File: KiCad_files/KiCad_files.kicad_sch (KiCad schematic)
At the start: 54 parts, among them J1 Conn_01x02_Socket, J10 Conn_01x01_Pin, J11 Conn_01x01_Pin, J6 Conn_01x01_Socket, J7 Conn_01x01_Socket, J8 Conn_01x01_Socket, J9 Conn_01x01_Socket, SW1 SW_Omron_B3FS, U2 LM22670QMR-5.0, U3 MC33275ST-3.3T3G, U4 ADM3488ExR

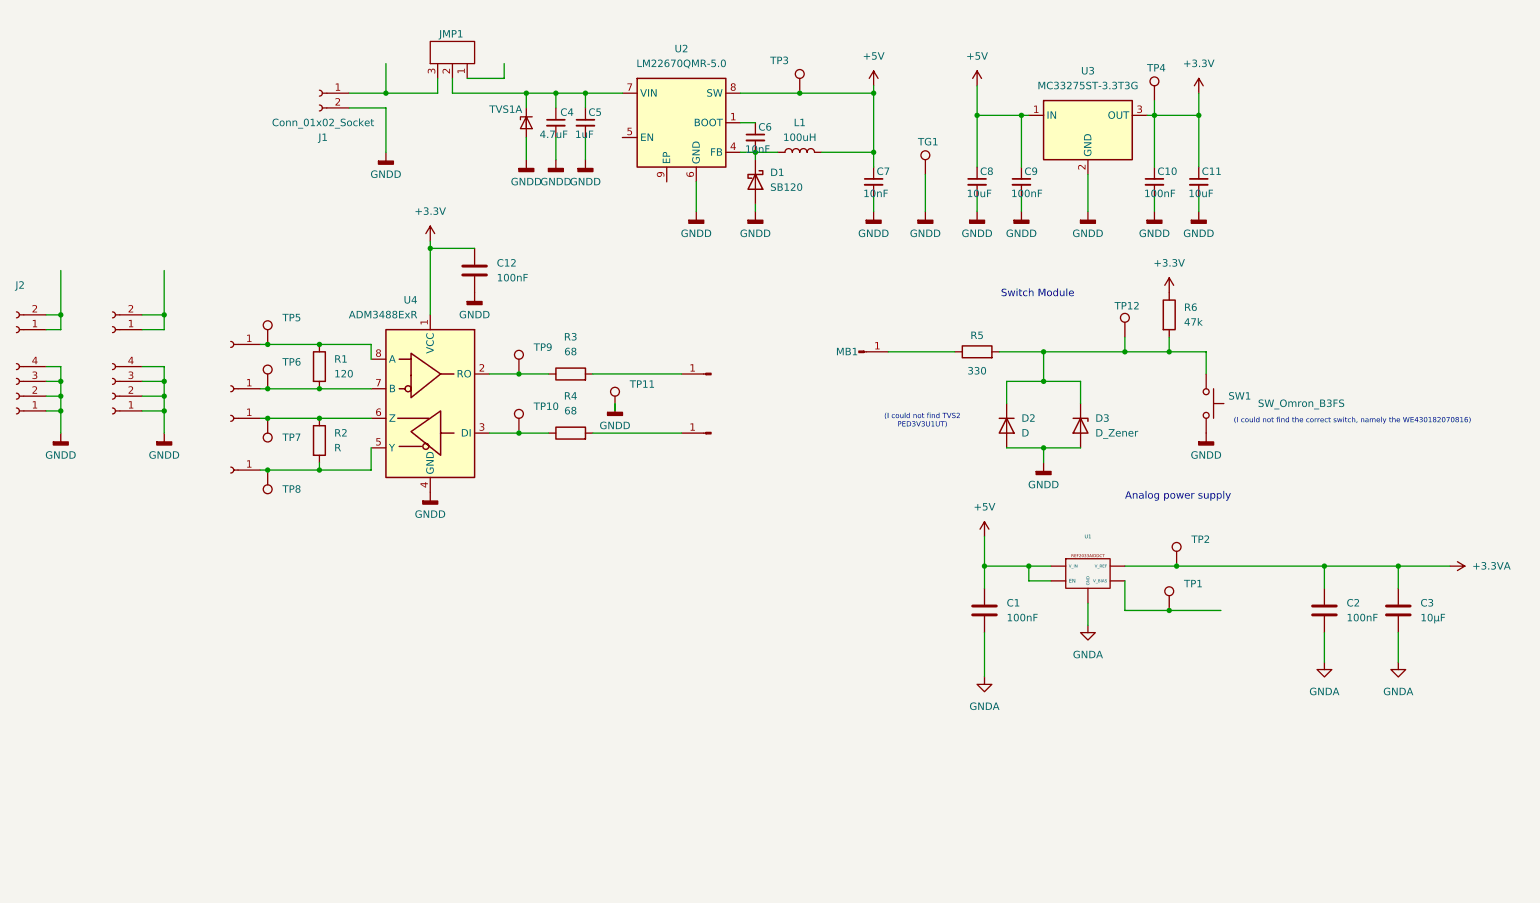
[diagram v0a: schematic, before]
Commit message: Made the schematic somewhat presentable and filled out the last bit of the circuit
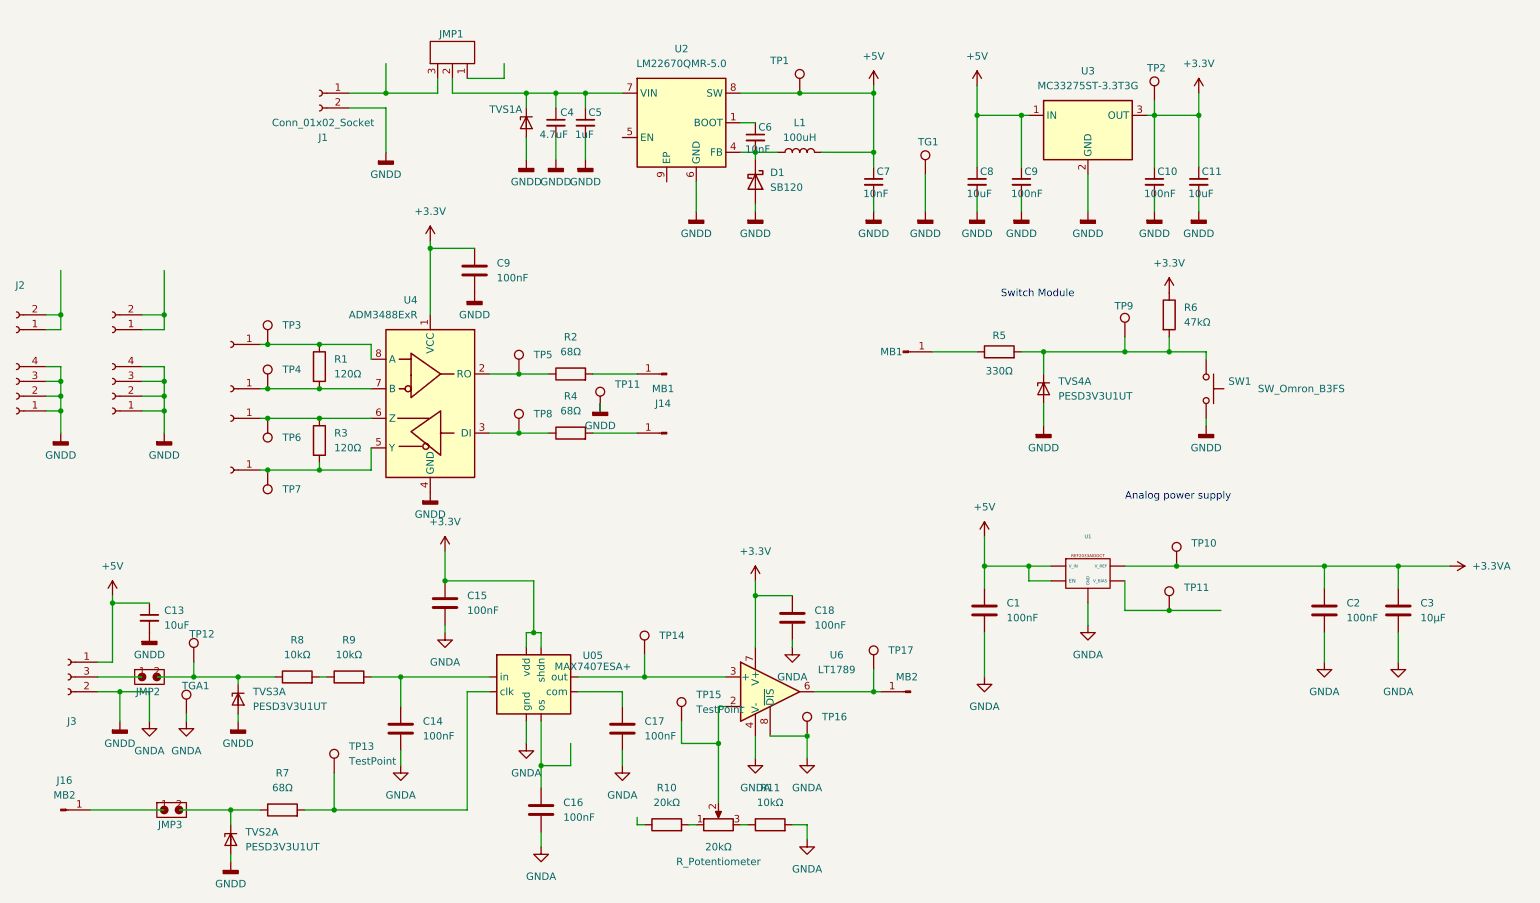
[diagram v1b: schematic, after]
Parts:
- removed D2: D, symbol Device:D
- removed D3: D_Zener, symbol Device:D_Zener
- added 20kΩ: R_Potentiometer, symbol Device:R_Potentiometer
- added C13: 10uF, symbol Device:C_Small
- added C14, C15, C16, C17, C18: 100nF, symbol Device:C
- added J16: MB2, symbol Connector:Conn_01x01_Pin
- added J3: Conn_01x03_Socket, symbol Connector:Conn_01x03_Socket
- added JMP2, JMP3: ~, symbol New_Library:2pin_jumper
- added MB2: Conn_01x01_Pin, symbol Connector:Conn_01x01_Pin
- added R10: 20kΩ, symbol Device:R
- added R11, R8, R9: 10kΩ, symbol Device:R
- added R7: 68Ω, symbol Device:R
- added TGA1, TP12, TP13, TP14, TP15, TP16, TP17: TestPoint, symbol Connector:TestPoint
- added TVS2, TVS3, TVS4: PESD3V3U1UT, Package_TO_SOT_SMD:SOT-23, symbol Power_Protection:PESD3V3L4UF
- added U6: LT1789, Package_SO:SOIC-8_3.9x4.9mm_P1.27mm, symbol Amplifier_Operational:OPA690xD
- J13: renamed from J11; value Conn_01x01_Pin -> MB1
- J14: renamed from J10; value Conn_01x01_Pin -> MB1
- R1: value 120 -> 120Ω
- R2: renamed from R3; value 68 -> 68Ω
- R3: renamed from R2; value R -> 120Ω
- R4: value 68 -> 68Ω
- R5: value 330 -> 330Ω
- R6: value 47k -> 47kΩ
- renumbered C12 to C9, TP3 to TP1, TP2 to TP10, TP1 to TP11, TP4 to TP2, TP5 to TP3, TP6 to TP4, TP9 to TP5, TP7 to TP6, TP8 to TP7, TP10 to TP8, TP12 to TP9
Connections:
- net GNDD is gone; now on net GNDA: C10.2, C11.2, C4.2, C5.2, C7.2, C8.2, C9.2, C9.2, D1.2 (A), J1.2 (Pin_2), J3.1 (Pin_1), J3.2 (Pin_2), J3.3 (Pin_3), J3.4 (Pin_4), J5.1 (Pin_1), J5.2 (Pin_2), J5.3 (Pin_3), J5.4 (Pin_4), SW1.2, TG1.1, TP11.1, TVS1.2 (A), TVS1.5 (A), U2.6 (GND), U3.2 (GND), U4.4 (GND)
- net +3.3V: now also C15.1, C18.1, U6.7 (V+)
- net +5V: now also C13.1, J3.1 (Pin_1)
- net GNDA: now also C13.2, C14.2, C15.2, C16.2, C17.2, C18.2, J3.2 (Pin_3), R11.2, TGA1.1, TP16.1, TVS2.2 (A), TVS2.5 (A), TVS3.2 (A), TVS3.5 (A), TVS4.2 (A), TVS4.5 (A), U6.4 (V-), U6.8 (~{DIS})
- net at R5.2, R6.2, SW1.1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: now also TVS4.1 (K1)
- new net: JMP3.2, R7.1, TVS2.1 (K1)
- new net: J3.3 (Pin_2), JMP2.1
- new net: JMP2.2, R8.1, TP12.1, TVS3.1 (K1)
- new net: MB2.1 (Pin_1), TP17.1, U6.6
- new net: R7.2, TP13.1
- new net: J16.1 (Pin_1), JMP3.1
- new net: R8.2, R9.1
- new net: 20kΩ.2, TP15.1, U6.2 (-)
- new net: TP14.1, U6.3 (+)
- new net: 20kΩ.3, R11.1
- new net: 20kΩ.1, R10.2
- new net: C14.1, R9.2
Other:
- note removed: "(I could not find TVS2 PED3V3U1UT)"
- note removed: "(I could not find the correct switch, namely the WE430182070816)"
- moved on the sheet: MB1, R5, SW1, TP11

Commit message: SchematicEdits
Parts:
- added J10, J8, J9: MB1, symbol Connector:Conn_01x01_Pin
- added J10, J8, J9: MB2, symbol Connector:Conn_01x01_Pin
- added TP18: 5V, symbol Connector:TestPoint
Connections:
- net GNDA: now also J8.1 (Pin_1), J8.1 (Pin_1), J9.1 (Pin_1), J9.1 (Pin_1)
- new net: J10.1 (Pin_1), J10.1 (Pin_1), TP18.1
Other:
- company: (none) -> ELE340-Elektronikkutvikling og Systemkonstruksjon
- title: (none) -> Schematic Drawing Proposal

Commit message: i inserted some footprints
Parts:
- removed C4: 4.7uF, symbol Device:C_Small
- removed C9: 100nF, symbol Device:C
- removed J10, J8, J9: MB1, symbol Connector:Conn_01x01_Pin
- removed J10, J8, J9: MB2, symbol Connector:Conn_01x01_Pin
- removed J2: ~, symbol Connector:Conn_01x02_Socket
- removed J3: ~, symbol Connector:Conn_01x04_Socket
- removed TP11: TestPoint, symbol Connector:TestPoint
- removed U2: LM22670QMR-5.0, Package_SO:SOIC-8-1EP_3.9x4.9mm_P1.27mm_EP2.29x3mm, symbol Regulator_Switching:LM22676MR-5
- removed U3: MC33275ST-3.3T3G, Package_TO_SOT_SMD:SOT-223, symbol Regulator_Linear:LT1963AxST-3.3
- removed U4: ADM3488ExR, Package_SO:SOIC-8_3.9x4.9mm_P1.27mm, symbol Interface_UART:ADM3488ExR
- added C12: 10uF, Capacitor_SMD:C_1210_3225Metric_Pad1.33x2.70mm_HandSolder, symbol Device:C_Small
- added C4: 100nF, symbol Device:C
- added J10: Conn_01x02_Socket, symbol Connector:Conn_01x02_Socket
- added J11, J15, J17: MB1, symbol Connector:Conn_01x01_Pin
- added J12, J18, J19: MB2, symbol Connector:Conn_01x01_Pin
- added J2: ~, symbol Connector:Conn_01x04_Socket
- added TP19: TestPoint, symbol Connector:TestPoint
- added U2: ADM3488ExR, Package_SO:SOIC-8_3.9x4.9mm_P1.27mm, symbol Interface_UART:ADM3488ExR
- added U3: LM22670QMR-5.0, Package_SO:SOIC-8-1EP_3.9x4.9mm_P1.27mm_EP2.29x3mm, symbol Regulator_Switching:LM22676MR-5
- added U4: MC33275ST-3.3T3G, Package_TO_SOT_SMD:SOT-223, symbol Regulator_Linear:LT1963AxST-3.3
- C10, C7: footprint (none) -> Capacitor_SMD:C_1206_3216Metric_Pad1.33x1.80mm_HandSolder
- C11: value 10uF -> 100nF; footprint (none) -> Capacitor_SMD:C_1206_3216Metric_Pad1.33x1.80mm_HandSolder
- C5: value 1uF -> 4.7uF; footprint (none) -> Capacitor_SMD:C_1206_3216Metric_Pad1.33x1.80mm_HandSolder
- C6: value 10nF -> 1uF; footprint (none) -> Capacitor_SMD:C_1206_3216Metric_Pad1.33x1.80mm_HandSolder
- C8: value 10uF -> 10nF; footprint (none) -> Capacitor_SMD:C_1206_3216Metric_Pad1.33x1.80mm_HandSolder
- C9: value 100nF -> 10uF; footprint (none) -> Capacitor_SMD:C_1210_3225Metric_Pad1.33x2.70mm_HandSolder
- J1: value Conn_01x02_Socket -> ~
- JMP1: footprint (none) -> Jumper:Pin_Header_2x1_P2.54mm_Vertical
- R1, R4: footprint (none) -> Resistor_SMD:R_1206_3216Metric_Pad1.30x1.75mm_HandSolder
- R2: value 68Ω -> 120Ω; footprint (none) -> Resistor_SMD:R_1206_3216Metric_Pad1.30x1.75mm_HandSolder
- R3: value 120Ω -> 68Ω; footprint (none) -> Resistor_SMD:R_1206_3216Metric_Pad1.30x1.75mm_HandSolder
- TP18: value 5V -> TestPoint
- TP7: value TestPoint -> 5V
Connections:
- net +3.3V: now also C12.1, C4.1, TP19.1, U2.1 (VCC), U4.3 (OUT); no longer C10.1, TP2.1
- net +5V: now also C10.1, TP18.1, U3.8 (SW), U4.1 (IN); no longer C7.1, TP1.1
- net GNDA: now also C6.2, TP8.1, C12.2, C4.2, J10.2 (Pin_2), J15.1 (Pin_1), J17.1 (Pin_1), J18.1 (Pin_1), J19.1 (Pin_1), J2.1 (Pin_1), J2.2 (Pin_2), J2.3 (Pin_3), J2.4 (Pin_4), U2.4 (GND), U3.6 (GND), U4.2 (GND); no longer C7.2, J1.2 (Pin_2)
- net at R4.1: now also TP6.1, U2.3 (DI); no longer TP8.1
- net at J13.1 (Pin_1): now also R3.2; no longer R4.2
- net at J6.1 (Pin_1), R1.1: now also TP1.1, U2.8 (A); no longer TP3.1
- net at J7.1 (Pin_1), R1.2: now also TP2.1, U2.7 (B); no longer TP4.1
- net at R2.1: now also J8.1 (Pin_1), TP3.1, U2.6 (Z); no longer TP5.1
- net at R2.2: now also J9.1 (Pin_1), TP4.1, U2.5 (Y); no longer J14.1 (Pin_1)
- net at C5.1, JMP1.2, TVS1.1 (K1): now also C6.1, U3.7 (VIN)
- net at J1.1 (Pin_1): now also J1.2 (Pin_2); no longer JMP1.3
- net at D1.1 (K), L1.1: now also C7.2, U3.4 (FB); no longer C6.2
- new net: R3.1, TP5.1, U2.2 (RO)
- new net: C7.1, U3.1 (BOOT)
- new net: J11.1 (Pin_1), J12.1 (Pin_1), TP7.1
- new net: J10.1 (Pin_1), JMP1.3
- new net: J14.1 (Pin_1), R4.2

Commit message: added L footprint
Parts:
- L1: footprint (none) -> The_prittiest_library:SDR2207
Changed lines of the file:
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@@
 			)
 		)
-		(property "Footprint" ""
+		(property "Footprint" "The_prittiest_library:SDR2207"
 			(at 156.21 43.18 0)
 			(effects

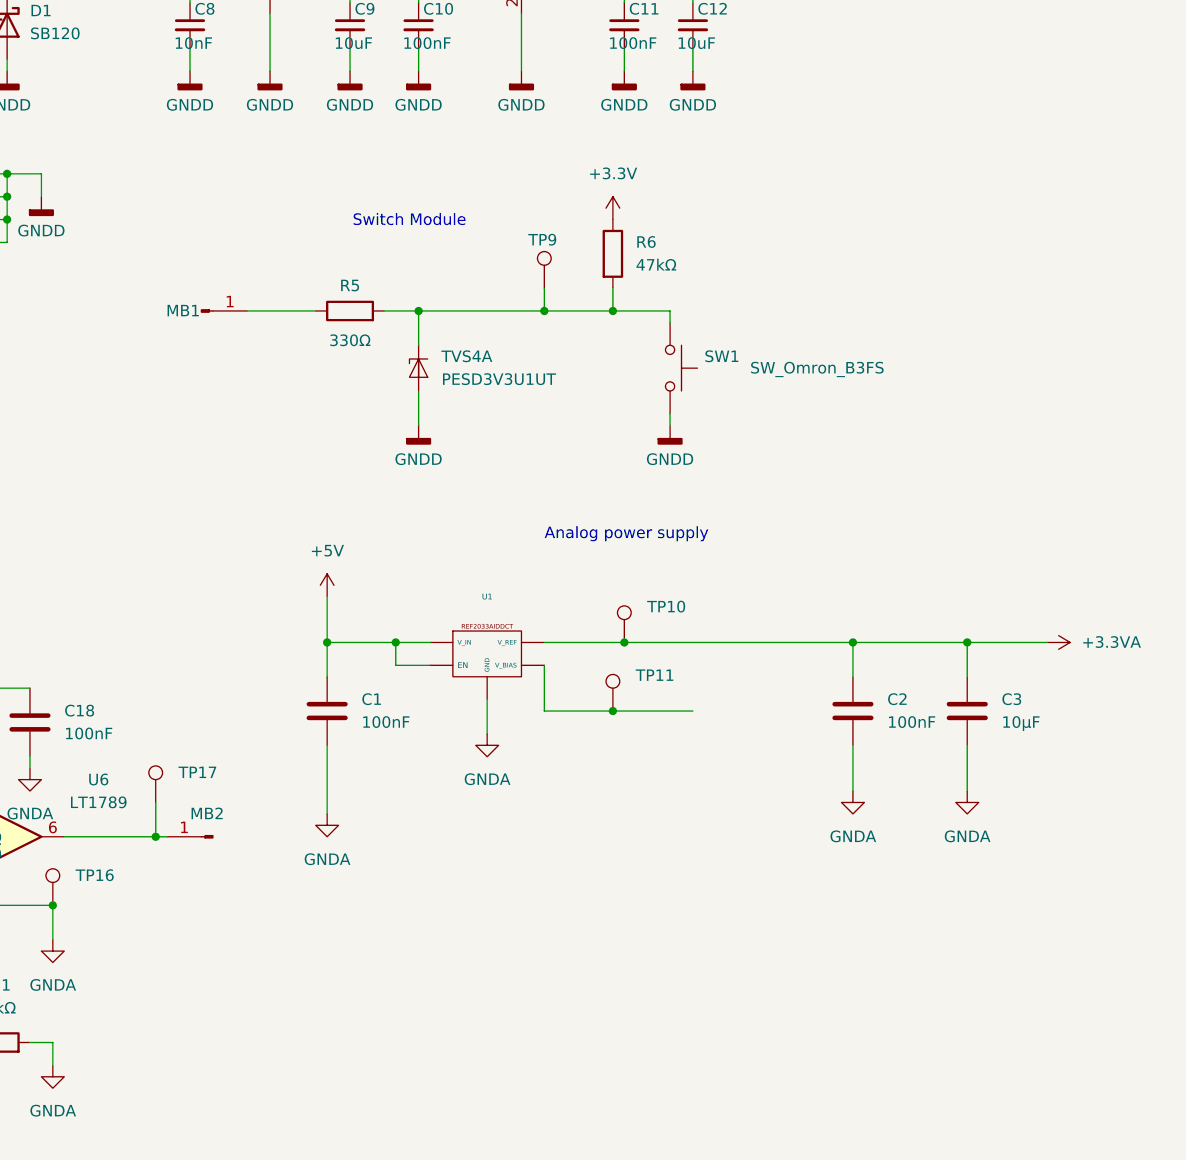
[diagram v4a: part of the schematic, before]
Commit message: changed the switch and what's under it
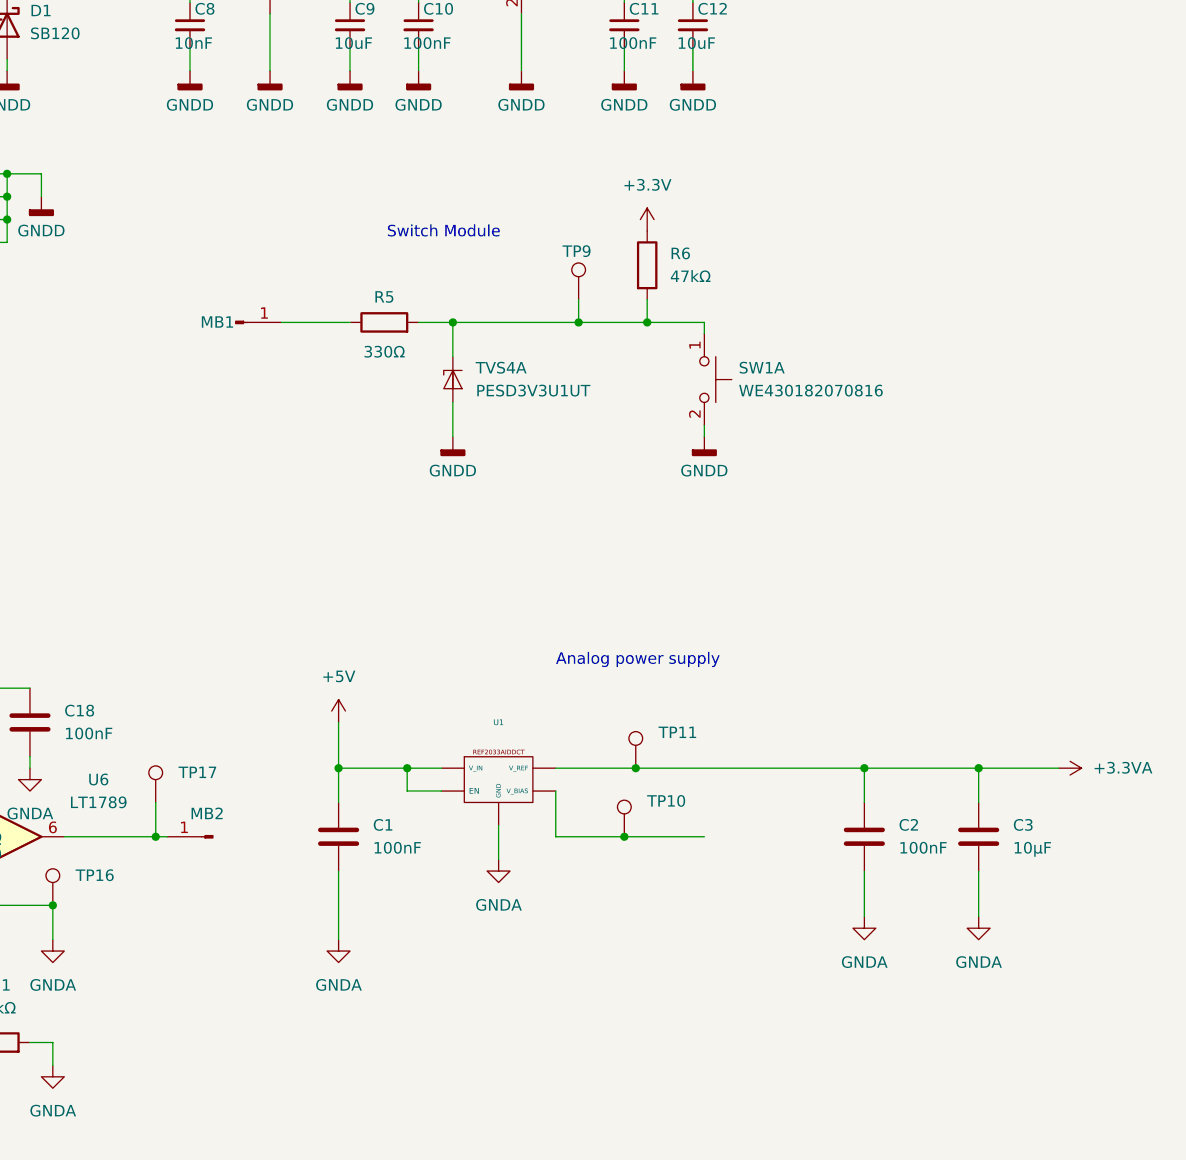
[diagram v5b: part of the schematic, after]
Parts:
- removed SW1: SW_Omron_B3FS, symbol Switch:SW_Omron_B3FS
- added SW1: WE430182070816, MyLibrary1:Switch WE430182070816, symbol Switch:SW_Push_Dual_x2
- C1, C2, C3: footprint (none) -> Capacitor_SMD:C_1206_3216Metric_Pad1.33x1.80mm_HandSolder
- R5, R6: footprint (none) -> Resistor_SMD:R_1206_3216Metric_Pad1.30x1.75mm_HandSolder
- U1: footprint (none) -> SOT-23-5
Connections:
- net +3.3VA: now also TP11.1; no longer TP10.1
- net GNDA: now also SW1.2 (D)
- net at R5.2, R6.2, TP9.1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: now also SW1.1 (C)
- new net: TP10.1, U1. (V_REF)

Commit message: meme
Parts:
- renumbered 20kΩ to 20kΩ1
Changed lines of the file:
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@@
 		(dnp no)
 		(fields_autoplaced yes)
-		(property "Reference" "U05"
+		(property "Reference" "#U05"
 			(at 116.84 132.2068 0)
 			(effects
@@
 			(project "KiCad_files"
 				(path "/f93895fa-12b9-4ad7-81f4-36be00b56edd"
-					(reference "U05")
+					(reference "#U05")
 					(unit 1)
 				)
@@
 		(dnp no)
 		(fields_autoplaced yes)
-		(property "Reference" "20kΩ"
+		(property "Reference" "20kΩ1"
 			(at 138.43 165.1 90)
 			(effects
@@
 			(project "KiCad_files"
 				(path "/f93895fa-12b9-4ad7-81f4-36be00b56edd"
-					(reference "20kΩ")
+					(reference "20kΩ1")
 					(unit 1)
 				)

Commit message: Added project library
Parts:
- L1: footprint The_prittiest_library:SDR2207 -> Library:SDR2207
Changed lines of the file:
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@@
 			)
 		)
-		(property "Footprint" "The_prittiest_library:SDR2207"
+		(property "Footprint" "Library:SDR2207"
 			(at 156.21 43.18 0)
 			(effects

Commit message: added footprint for pin headers and updated footprints
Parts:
- JMP2, JMP3: footprint (none) -> Library:Pin_Header_2x1_P2.54mm_Vertical
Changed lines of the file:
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@@
 			)
 		)
-		(property "Footprint" ""
+		(property "Footprint" "Library:Pin_Header_2x1_P2.54mm_Vertical"
 			(at 40.64 135.89 0)
 			(effects
@@
 			)
 		)
-		(property "Footprint" ""
+		(property "Footprint" "Library:Pin_Header_2x1_P2.54mm_Vertical"
 			(at 44.45 158.75 0)
 			(effects
